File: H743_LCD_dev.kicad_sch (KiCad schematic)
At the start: 0 parts

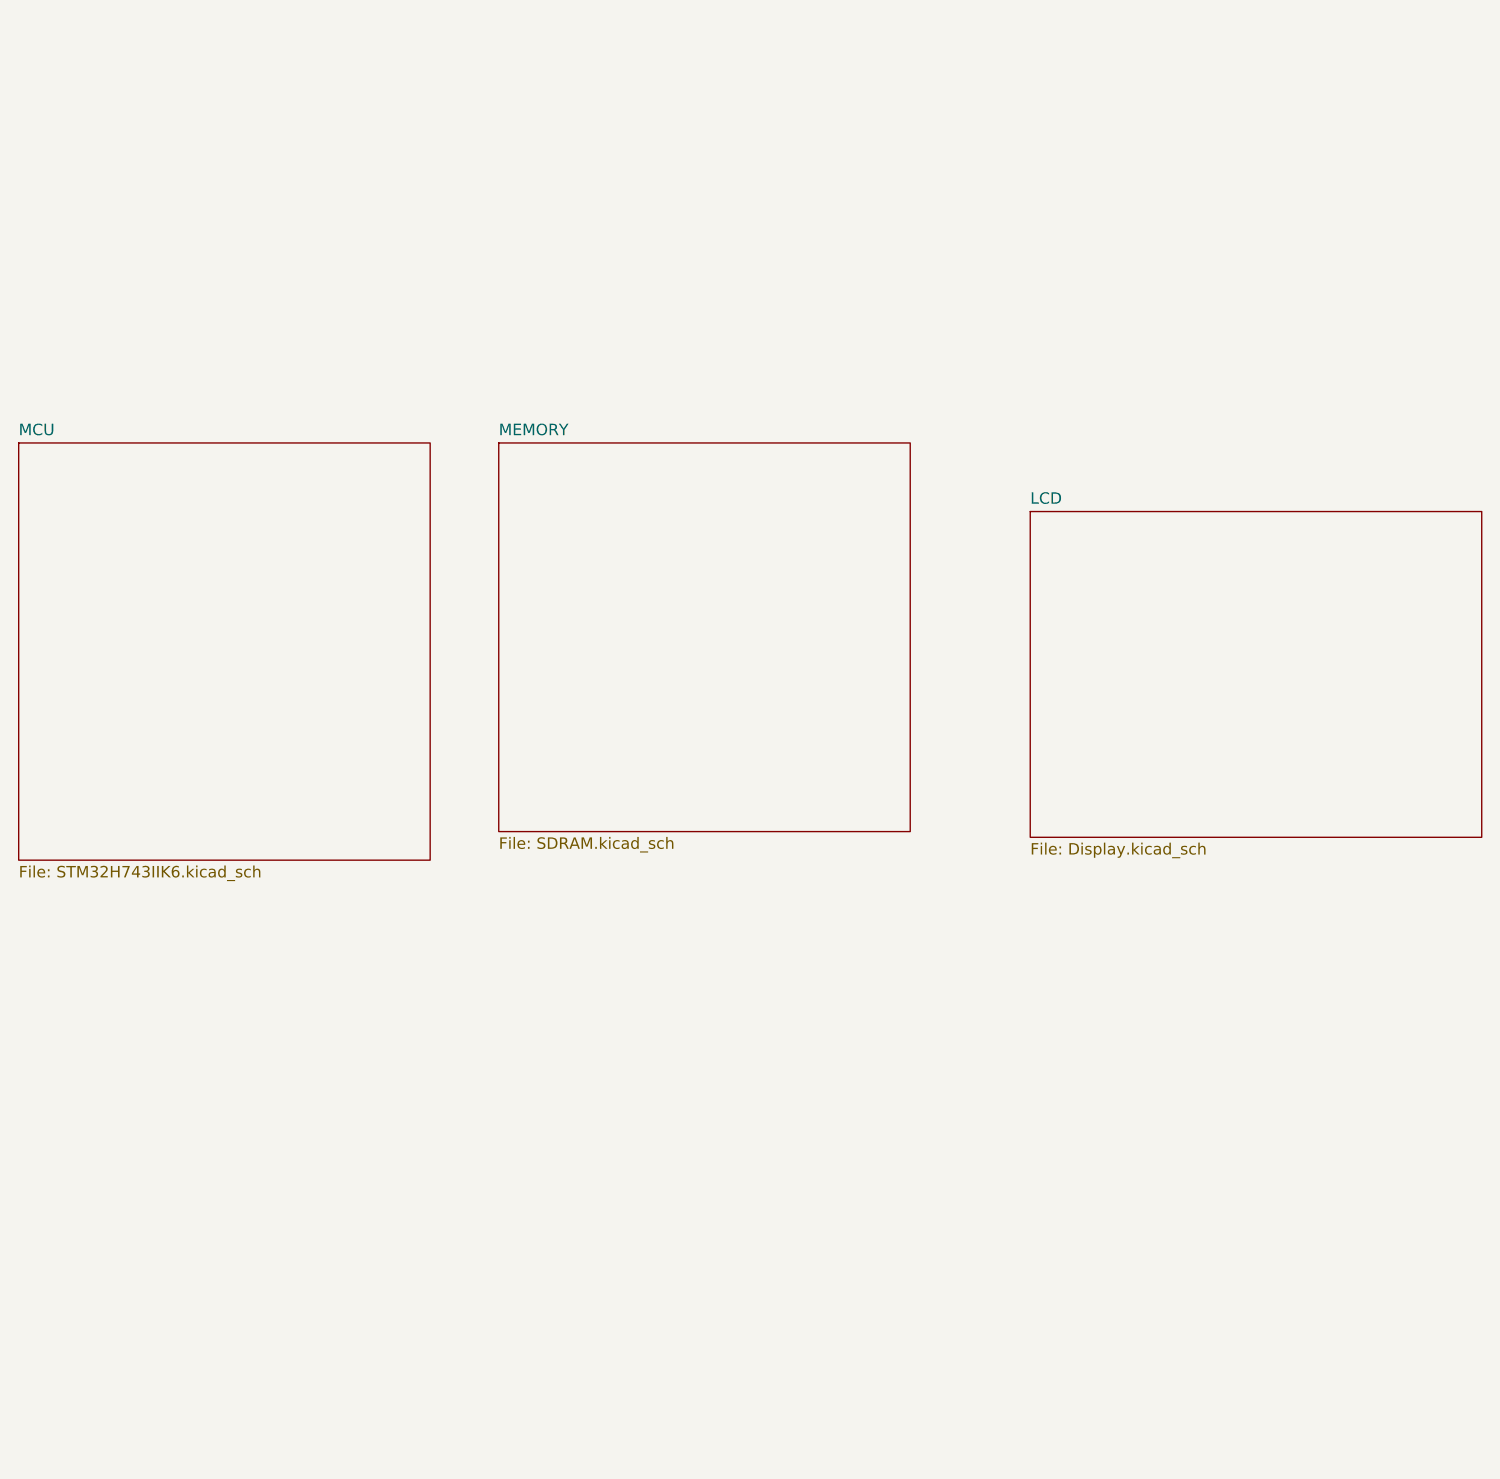
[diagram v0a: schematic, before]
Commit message: Added UART, i2c, debug, NAND Flash, NOR Flash, EEPROM, SD-Card
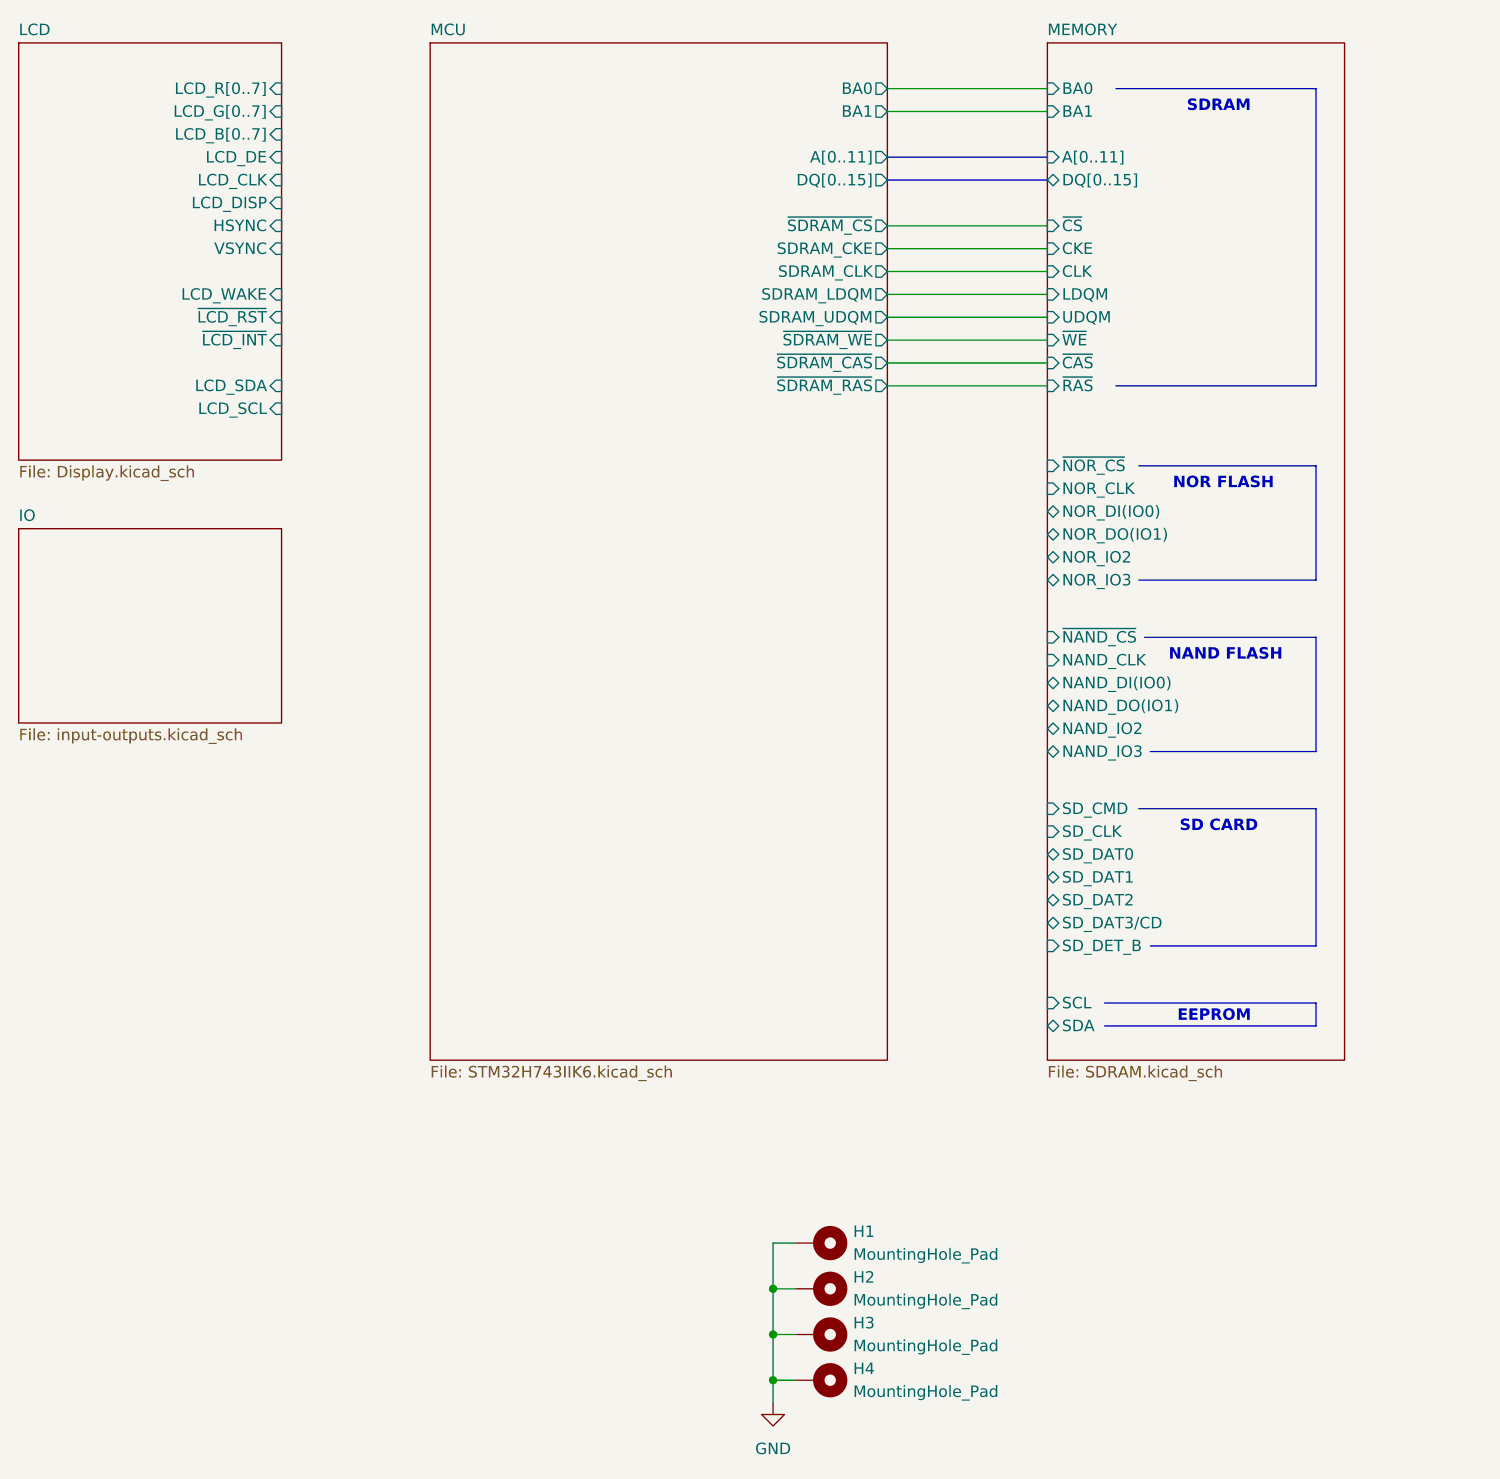
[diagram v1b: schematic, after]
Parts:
- added H1, H2, H3, H4: MountingHole_Pad, MountingHole:MountingHole_3.2mm_M3_Pad_Via, symbol Mechanical:MountingHole_Pad
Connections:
- new net GND: H1.1, H2.1, H3.1, H4.1
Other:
- added sheet IO (input-outputs.kicad_sch)
- sheet LCD ports: added HSYNC, LCD_B[0..7], LCD_CLK, LCD_DE, LCD_DISP, LCD_G[0..7], LCD_R[0..7], LCD_SCL, LCD_SDA, LCD_WAKE, VSYNC, ~{LCD_INT}, ~{LCD_RST}; removed none
- sheet MCU ports: added A[0..11], BA0, BA1, DQ[0..15], SDRAM_CKE, SDRAM_CLK, SDRAM_LDQM, SDRAM_UDQM, ~{SDRAM_CAS}, ~{SDRAM_CS}, ~{SDRAM_RAS}, ~{SDRAM_WE}; removed none
- sheet MEMORY ports: added A[0..11], BA0, BA1, CKE, CLK, DQ[0..15], LDQM, NAND_CLK, NAND_DI(IO0), NAND_DO(IO1), NAND_IO2, NAND_IO3, NOR_CLK, NOR_DI(IO0), NOR_DO(IO1), NOR_IO2, NOR_IO3, SCL, SDA, SD_CLK, SD_CMD, SD_DAT0, SD_DAT1, SD_DAT2, SD_DAT3/CD, SD_DET_B, UDQM, ~{CAS}, ~{CS}, ~{NAND_CS}, ~{NOR_CS}, ~{RAS}, ~{WE}; removed none
- note added: "EEPROM"
- note added: "NAND FLASH"
- note added: "NOR FLASH"
- note added: "SD CARD"
- note added: "SDRAM"

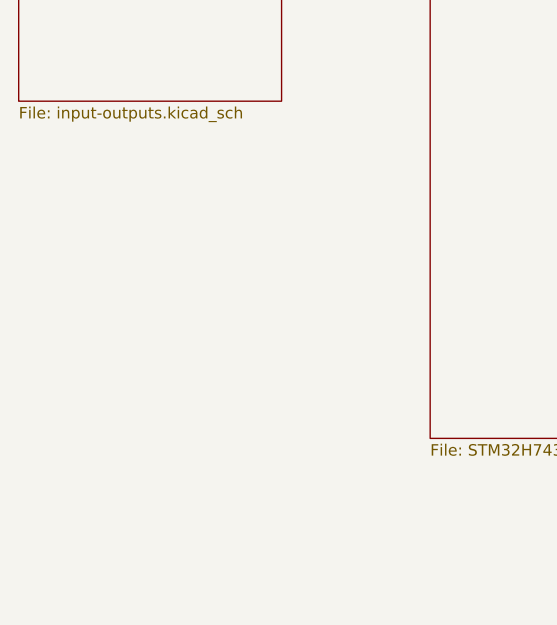
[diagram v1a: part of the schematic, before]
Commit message: Added I2S Audio amplifier
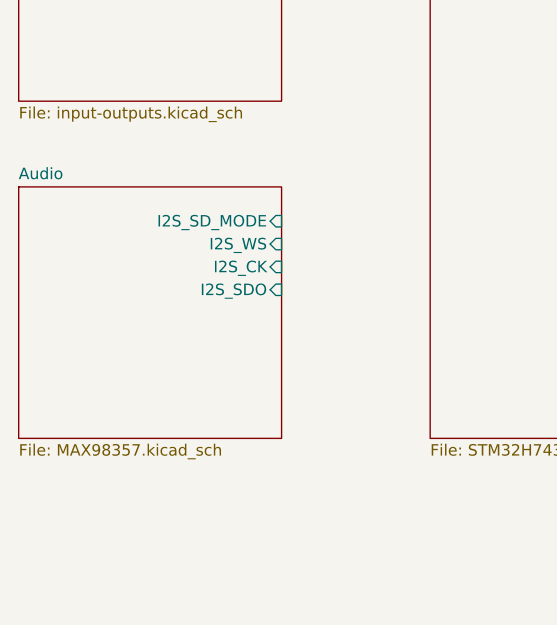
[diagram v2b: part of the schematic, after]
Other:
- added sheet Audio (MAX98357.kicad_sch)
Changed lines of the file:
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@@
+	)
+	(sheet
+		(at 58.42 111.76)
+		(size 29.21 27.94)
+		(fields_autoplaced yes)
+		(stroke
+			(width 0.1524)
+			(type solid)
+		)
+		(fill
+			(color 0 0 0 0.0000)
+		)
+		(property "Sheetname" "Audio"
+			(at 58.42 111.0484 0)
+			(effects
+				(font
+					(size 1.27 1.27)
+				)
+				(justify left bottom)
+			)
+		)
+		(property "Sheetfile" "MAX98357.kicad_sch"
+			(at 58.42 140.2846 0)
+			(effects
+				(font
+					(size 1.27 1.27)
+				)
+				(justify left top)
+			)
+		)
+		(pin "I2S_SD_MODE" input
+			(at 87.63 115.57 0)
+			(effects
+				(font
+					(size 1.27 1.27)
+				)
+				(justify right)
+			)
+		)
+		(pin "I2S_WS" input
+			(at 87.63 118.11 0)
+			(effects
+				(font
+					(size 1.27 1.27)
+				)
+				(justify right)
+			)
+		)
+		(pin "I2S_SDO" input
+			(at 87.63 123.19 0)
+			(effects
+				(font
+					(size 1.27 1.27)
+				)
+				(justify right)
+			)
+		)
+		(pin "I2S_CK" input
+			(at 87.63 120.65 0)
+			(effects
+				(font
+					(size 1.27 1.27)
+				)
+				(justify right)
+			)
+		)
+		(instances
+			(project "H743_LCD_dev"
+				(path "/70094798-b7e4-48a4-a512-b8f48be18f9f"
+					(page "6")
+				)
+			)
+		)
 	)
 	(sheet

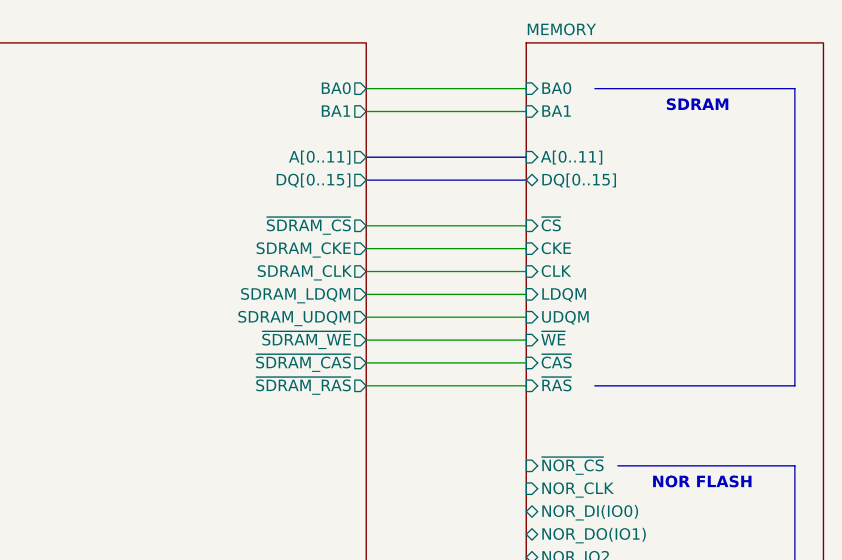
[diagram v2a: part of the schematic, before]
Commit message: Finish high speed sdram tracks
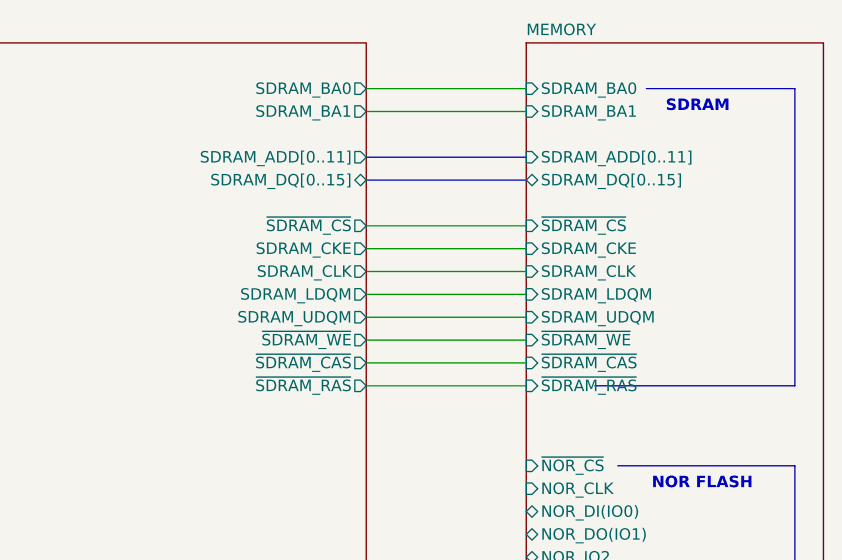
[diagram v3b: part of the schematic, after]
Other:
- sheet MCU ports: added SDRAM_ADD[0..11], SDRAM_BA0, SDRAM_BA1, SDRAM_DQ[0..15]; removed A[0..11], BA0, BA1, DQ[0..15]
- sheet MEMORY ports: added SDRAM_ADD[0..11], SDRAM_BA0, SDRAM_BA1, SDRAM_CKE, SDRAM_CLK, SDRAM_DQ[0..15], SDRAM_LDQM, SDRAM_UDQM, ~{SDRAM_CAS}, ~{SDRAM_CS}, ~{SDRAM_RAS}, ~{SDRAM_WE}; removed A[0..11], BA0, BA1, CKE, CLK, DQ[0..15], LDQM, UDQM, ~{CAS}, ~{CS}, ~{RAS}, ~{WE}
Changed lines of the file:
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@@
 	(polyline
 		(pts
-			(xy 180.34 31.75) (xy 202.565 31.75)
+			(xy 186.055 31.75) (xy 202.565 31.75)
 		)
 		(stroke
@@
 			)
 		)
-		(pin "A[0..11]" output
-			(at 154.94 39.37 0)
-			(effects
-				(font
-					(size 1.27 1.27)
-				)
-				(justify right)
-			)
-		)
-		(pin "DQ[0..15]" output
-			(at 154.94 41.91 0)
-			(effects
-				(font
-					(size 1.27 1.27)
-				)
-				(justify right)
-			)
-		)
 		(pin "~{SDRAM_RAS}" output
 			(at 154.94 64.77 0)
@@
 			)
 		)
-		(pin "BA1" output
-			(at 154.94 34.29 0)
-			(effects
-				(font
-					(size 1.27 1.27)
-				)
-				(justify right)
-			)
-		)
-		(pin "BA0" output
-			(at 154.94 31.75 0)
-			(effects
-				(font
-					(size 1.27 1.27)
-				)
-				(justify right)
-			)
-		)
 		(pin "SDRAM_CLK" output
 			(at 154.94 52.07 0)
@@
 		(pin "~{SDRAM_CAS}" output
 			(at 154.94 62.23 0)
+			(effects
+				(font
+					(size 1.27 1.27)
+				)
+				(justify right)
+			)
+		)
+		(pin "SDRAM_DQ[0..15]" bidirectional
+			(at 154.94 41.91 0)
+			(effects
+				(font
+					(size 1.27 1.27)
+				)
+				(justify right)
+			)
+		)
+		(pin "SDRAM_ADD[0..11]" output
+			(at 154.94 39.37 0)
+			(effects
+				(font
+					(size 1.27 1.27)
+				)
+				(justify right)
+			)
+		)
+		(pin "SDRAM_BA0" output
+			(at 154.94 31.75 0)
+			(effects
+				(font
+					(size 1.27 1.27)
+				)
+				(justify right)
+			)
+		)
+		(pin "SDRAM_BA1" output
+			(at 154.94 34.29 0)
 			(effects
 				(font
@@
 			)
 		)
-		(pin "DQ[0..15]" bidirectional
-			(at 172.72 41.91 180)
-			(effects
-				(font
-					(size 1.27 1.27)
-				)
-				(justify left)
-			)
-		)
-		(pin "CLK" input
-			(at 172.72 52.07 180)
-			(effects
-				(font
-					(size 1.27 1.27)
-				)
-				(justify left)
-			)
-		)
-		(pin "UDQM" input
-			(at 172.72 57.15 180)
-			(effects
-				(font
-					(size 1.27 1.27)
-				)
-				(justify left)
-			)
-		)
-		(pin "~{WE}" input
-			(at 172.72 59.69 180)
-			(effects
-				(font
-					(size 1.27 1.27)
-				)
-				(justify left)
-			)
-		)
-		(pin "LDQM" input
-			(at 172.72 54.61 180)
-			(effects
-				(font
-					(size 1.27 1.27)
-				)
-				(justify left)
-			)
-		)
-		(pin "~{CAS}" input
-			(at 172.72 62.23 180)
-			(effects
-				(font
-					(size 1.27 1.27)
-				)
-				(justify left)
-			)
-		)
-		(pin "~{RAS}" input
-			(at 172.72 64.77 180)
-			(effects
-				(font
-					(size 1.27 1.27)
-				)
-				(justify left)
-			)
-		)
-		(pin "~{CS}" input
-			(at 172.72 46.99 180)
-			(effects
-				(font
-					(size 1.27 1.27)
-				)
-				(justify left)
-			)
-		)
-		(pin "CKE" input
-			(at 172.72 49.53 180)
-			(effects
-				(font
-					(size 1.27 1.27)
-				)
-				(justify left)
-			)
-		)
-		(pin "A[0..11]" input
-			(at 172.72 39.37 180)
-			(effects
-				(font
-					(size 1.27 1.27)
-				)
-				(justify left)
-			)
-		)
-		(pin "BA0" input
-			(at 172.72 31.75 180)
-			(effects
-				(font
-					(size 1.27 1.27)
-				)
-				(justify left)
-			)
-		)
-		(pin "BA1" input
-			(at 172.72 34.29 180)
-			(effects
-				(font
-					(size 1.27 1.27)
-				)
-				(justify left)
-			)
-		)
 		(pin "SCL" input
 			(at 172.72 133.35 180)
@@
 			(effects
 				(font
+					(size 1.27 1.27)
+				)
+				(justify left)
+			)
+		)
+		(pin "SDRAM_BA0" input
+			(at 172.72 31.75 180)
+			(effects
+				(font
+					(size 1.27 1.27)
+				)
+				(justify left)
+			)
+		)
+		(pin "SDRAM_BA1" input
+			(at 172.72 34.29 180)
+			(effects
+				(font
+					(size 1.27 1.27)
+				)
+				(justify left)
+			)
+		)
+		(pin "SDRAM_DQ[0..15]" bidirectional
+			(at 172.72 41.91 180)
+			(effects
+				(font
+					(size 1.27 1.27)
+				)
+				(justify left)
+			)
+		)
+		(pin "SDRAM_ADD[0..11]" input
+			(at 172.72 39.37 180)
+			(effects
+				(font
+					(size 1.27 1.27)
+				)
+				(justify left)
+			)
+		)
+		(pin "SDRAM_CKE" input
+			(at 172.72 49.53 180)
+			(effects
+				(font
+					(size 1.27 1.27)
+				)
+				(justify left)
+			)
+		)
+		(pin "~{SDRAM_CS}" input
+			(at 172.72 46.99 180)
+			(effects
+				(font
+					(size 1.27 1.27)
+				)
+				(justify left)
+			)
+		)
+		(pin "~{SDRAM_RAS}" input
+			(at 172.72 64.77 180)
+			(effects
+				(font
+					(size 1.27 1.27)
+				)
+				(justify left)
+			)
+		)
+		(pin "~{SDRAM_CAS}" input
+			(at 172.72 62.23 180)
+			(effects
+				(font
+					(size 1.27 1.27)
+				)
+				(justify left)
+			)
+		)
+		(pin "SDRAM_CLK" input
+			(at 172.72 52.07 180)
+			(effects
+				(font
+					(size 1.27 1.27)
+				)
+				(justify left)
+			)
+		)
+		(pin "SDRAM_LDQM" input
+			(at 172.72 54.61 180)
+			(effects
+				(font
+					(size 1.27 1.27)
+				)
+				(justify left)
+			)
+		)
+		(pin "~{SDRAM_WE}" input
+			(at 172.72 59.69 180)
+			(effects
+				(font
+					(size 1.27 1.27)
+				)
+				(justify left)
+			)
+		)
+		(pin "SDRAM_UDQM" input
+			(at 172.72 57.15 180)
+			(effects
+				(font
